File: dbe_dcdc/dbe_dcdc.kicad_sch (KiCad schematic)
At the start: 33 parts, among them J1 PMBUS, Q1 MMBT3904, Q2 MMBT3904, U1 DBE0125V2NBC

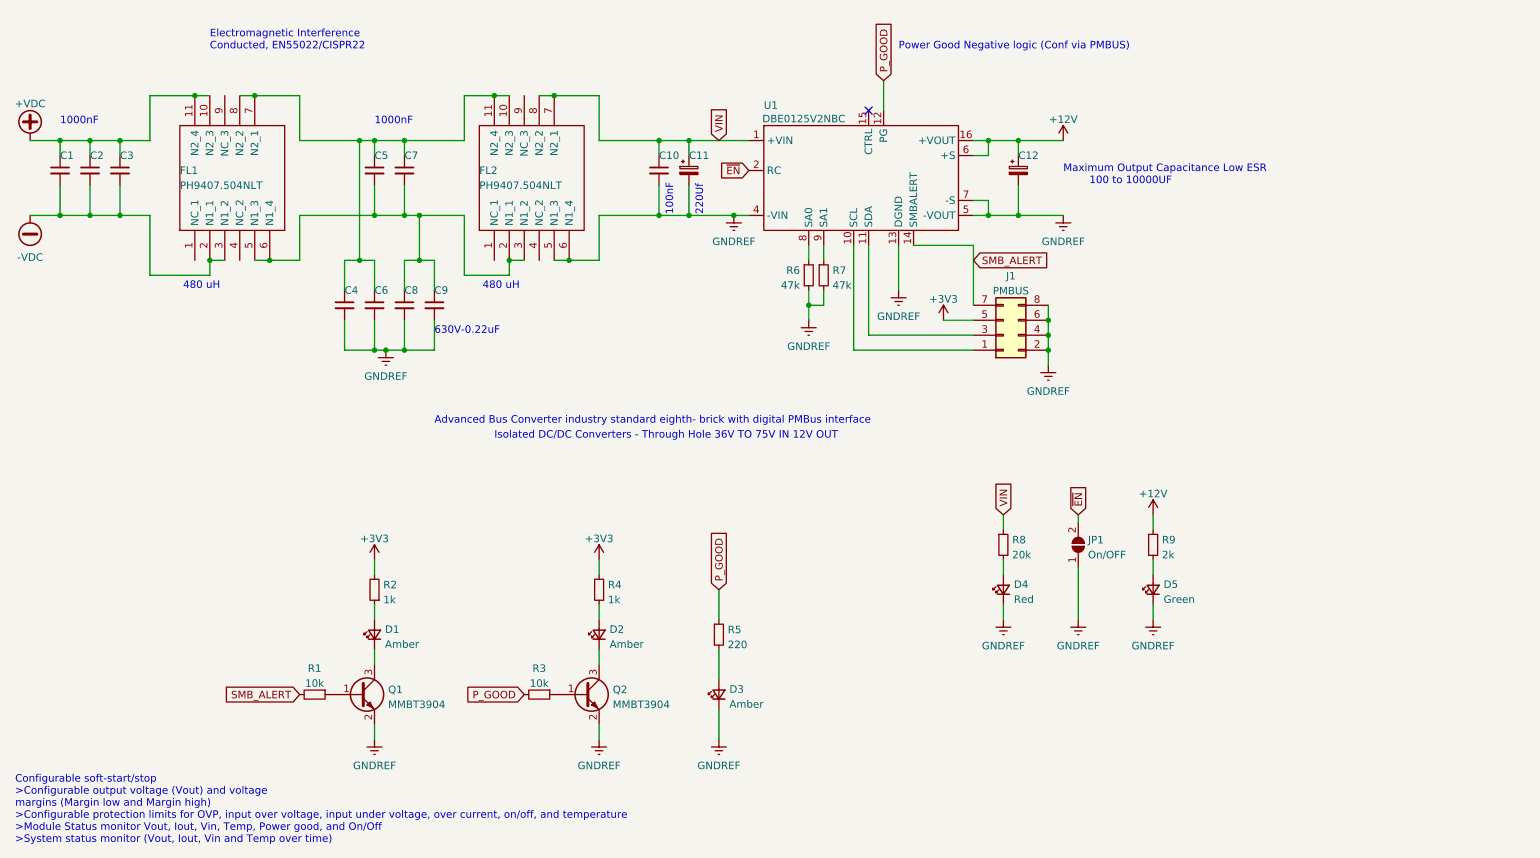
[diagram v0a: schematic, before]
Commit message: layout and schema changes for out and in filtering
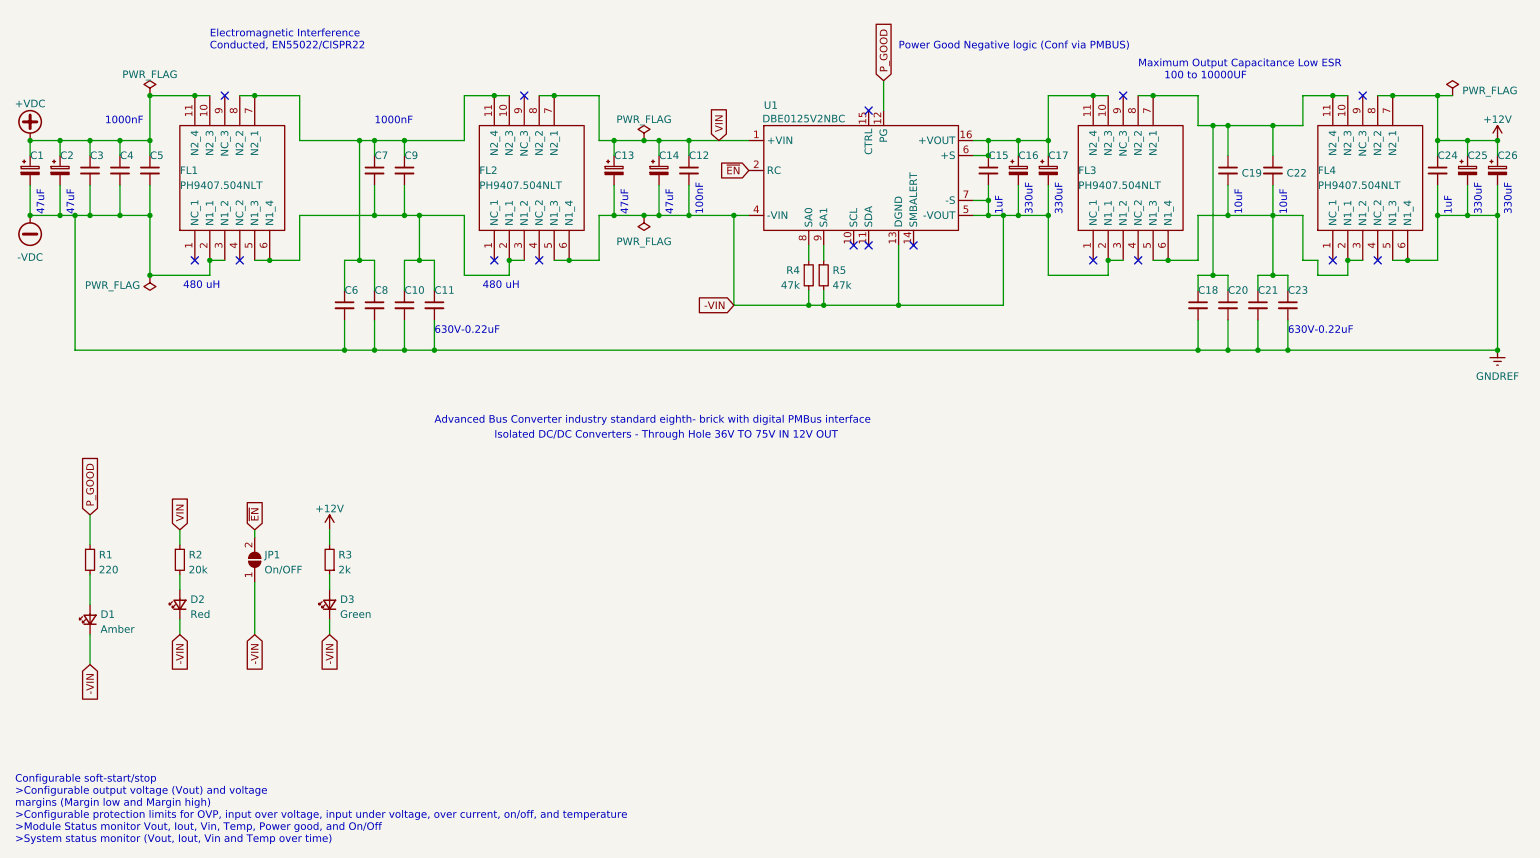
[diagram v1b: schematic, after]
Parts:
- removed D1, D2: Amber, LED_SMD:LED_0603_1608Metric_Pad1.05x0.95mm_HandSolder, symbol Device:LED_Small
- removed J1: PMBUS, Connector_PinHeader_2.54mm:PinHeader_2x04_P2.54mm_Vertical, symbol Connector_Generic:Conn_02x04_Odd_Even
- removed Q1, Q2: MMBT3904, Package_TO_SOT_SMD:SOT-23, symbol Transistor_BJT:MMBT3904
- removed R1, R3: 10k, Resistor_SMD:R_0805_2012Metric_Pad1.20x1.40mm_HandSolder, symbol Device:R_Small
- removed R2, R4: 1k, Resistor_SMD:R_0805_2012Metric_Pad1.20x1.40mm_HandSolder, symbol Device:R_Small
- added C1: 865080453014, Capacitor_SMD:CP_Elec_10x10.5, symbol Device:C_Polarized_Small
- added C13, C2: 865060857005, Capacitor_SMD:CP_Elec_10x10.5, symbol Device:C_Polarized_Small
- added C15: GCM21BR7YA105KA5L, Capacitor_SMD:C_1206_3216Metric_Pad1.33x1.80mm_HandSolder, symbol Device:C_Small
- added C17, C25, C26: 865080453014, Capacitor_SMD:CP_Elec_8x10.5, symbol Device:C_Polarized_Small
- added C18, C20, C21, C23: GRM55DR72J224KW01L, Capacitor_SMD:C_2220_5650Metric_Pad1.97x5.40mm_HandSolder, symbol Device:C_Small
- added C19, C22: GJ832ER7YA106KA2L, Capacitor_SMD:C_1210_3225Metric_Pad1.33x2.70mm_HandSolder, symbol Device:C_Small
- added C24: GCM21BR7YA105KA5L, Capacitor_SMD:C_1210_3225Metric_Pad1.33x2.70mm_HandSolder, symbol Device:C_Small
- added FL3, FL4: PH9407.504NLT, PH9407_504NLT:PH9407_504NLT, symbol PH9407_504NLT:PH9407.504NLT
- C14: renamed from C11; value UHE2A221MHD -> 865060857005; footprint Capacitor_THT:CP_Radial_D12.5mm_P5.00mm -> Capacitor_SMD:CP_Elec_10x10.5
- C16: renamed from C12; value NA -> 865080453014; footprint Capacitor_THT:CP_Radial_D12.5mm_P5.00mm -> Capacitor_SMD:CP_Elec_8x10.5; now in the parts list
- JP1: footprint Connector_PinHeader_2.54mm:PinHeader_2x01_P2.54mm_Vertical -> Jumper:SolderJumper-2_P1.3mm_Open_Pad1.0x1.5mm
- renumbered C8 to C10, C9 to C11, C10 to C12, C1 to C3, C2 to C4, C3 to C5, C4 to C6, C5 to C7, C6 to C8, C7 to C9, D3 to D1, D4 to D2, D5 to D3, R5 to R1, R8 to R2, R9 to R3, R6 to R4, R7 to R5
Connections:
- net +12V: now also C24.1, C25.1, C26.1, FL4.7 (N2_1), FL4.8 (N2_2); no longer C16.1, U1.16 (+VOUT), U1.6 (+S)
- net +VDC: now also C1.1, C2.1
- net -VDC: now also C10.2, C11.2, C6.2, C8.2, C1.2, C18.2, C2.2, C20.2, C21.2, C23.2, C24.2, C25.2, C26.2, FL4.5 (N1_3), FL4.6 (N1_4)
- net VIN: now also C13.1
- net GNDREF renamed -VIN
- net -VIN: now also C13.2, C15.2, C17.2, FL3.2 (N1_1), FL3.3 (N1_2); no longer C10.2, C11.2, C6.2, C8.2
- net SMB_ALERT: no longer names the net of U1.14 (SMBALERT)
- new net: C15.1, C16.1, C17.1, FL3.10 (N2_3), FL3.11 (N2_4), U1.16 (+VOUT), U1.6 (+S)
- new net: C18.1, C19.1, C20.1, C22.1, FL3.7 (N2_1), FL3.8 (N2_2), FL4.10 (N2_3), FL4.11 (N2_4)
- new net: C19.2, C21.1, C22.2, C23.1, FL3.5 (N1_3), FL3.6 (N1_4), FL4.2 (N1_1), FL4.3 (N1_2)
- no-connect marks 1 -> 16
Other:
- note added: "10uF"
- note added: "1uF"
- note added: "330uF"
- note added: "47uF"
- note removed: "220Uf"
- moved on the sheet: C12, C14, C3, C4, C5, D1, D2, D3, JP1, R1, R2, R3
